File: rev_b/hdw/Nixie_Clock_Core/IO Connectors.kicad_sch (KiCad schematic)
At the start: 0 parts

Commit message: more rev b sch progress
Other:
- note added: "FIND A CONNECTOR THAT CAN HANDLE HIGH VOLTAGE AND SIGNALLING THAT ISNT AWFUL CONSIDER USING 0.1" SMT HEADERS"
- note removed: "FIND A CONNECTOR THAT CAN HANDLE HIGH VOLTAGE AND SIGNALLING THAT ISNT AWFUL"
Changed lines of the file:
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@@
     (company "Drew Maatman")
   )
-  (text "FIND A CONNECTOR THAT CAN HANDLE HIGH VOLTAGE\nAND SIGNALLING THAT ISNT AWFUL"
-    (at 59.69 43.18 0)
+  (text "FIND A CONNECTOR THAT CAN HANDLE HIGH VOLTAGE\nAND SIGNALLING THAT ISNT AWFUL\n\nCONSIDER USING 0.1\" SMT HEADERS"
+    (at 36.83 48.26 0)
     (effects (font (face "Courier New") (size 5.08 5.08) (thickness 0.254) bold (color 255 37 56 1)) (justify left bottom))
   )
+  (global_label "Colon_3_DSP" (shape output) (at 54.61 162.56 0) (fields_autoplaced)
+    (effects (font (size 1.27 1.27)) (justify left))
+    (property "Intersheetrefs" "${INTERSHEET_REFS}" (at 69.7922 162.56 0)
+      (effects (font (size 1.27 1.27)) (justify left) hide)
+    )
+  )
+  (global_label "~{Display_Detect_DSP}" (shape input) (at 54.61 134.62 0)
+    (effects (font (size 1.016 1.016)) (justify left))
+    (property "Intersheetrefs" "${INTERSHEET_REFS}" (at 54.61 134.62 0)
+      (effects (font (size 1.27 1.27)) hide)
+    )
+  )
+  (global_label "Anode_6_DSP" (shape output) (at 54.61 101.6 0) (fields_autoplaced)
+    (effects (font (size 1.27 1.27)) (justify left))
+    (property "Intersheetrefs" "${INTERSHEET_REFS}" (at 70.0342 101.6 0)
+      (effects (font (size 1.27 1.27)) (justify left) hide)
+    )
+  )
+  (global_label "Colon_0_DSP" (shape output) (at 54.61 154.94 0) (fields_autoplaced)
+    (effects (font (size 1.27 1.27)) (justify left))
+    (property "Intersheetrefs" "${INTERSHEET_REFS}" (at 69.7922 154.94 0)
+      (effects (font (size 1.27 1.27)) (justify left) hide)
+    )
+  )
+  (global_label "Anode_4_DSP" (shape output) (at 54.61 96.52 0) (fields_autoplaced)
+    (effects (font (size 1.27 1.27)) (justify left))
+    (property "Intersheetrefs" "${INTERSHEET_REFS}" (at 70.0342 96.52 0)
+      (effects (font (size 1.27 1.27)) (justify left) hide)
+    )
+  )
+  (global_label "Anode_3_DSP" (shape output) (at 54.61 93.98 0) (fields_autoplaced)
+    (effects (font (size 1.27 1.27)) (justify left))
+    (property "Intersheetrefs" "${INTERSHEET_REFS}" (at 70.0342 93.98 0)
+      (effects (font (size 1.27 1.27)) (justify left) hide)
+    )
+  )
+  (global_label "I2C_DSP_SDA" (shape output) (at 54.61 113.03 0)
+    (effects (font (size 1.27 1.27)) (justify left))
+    (property "Intersheetrefs" "${INTERSHEET_REFS}" (at 54.61 113.03 0)
+      (effects (font (size 1.27 1.27)) hide)
+    )
+  )
+  (global_label "Pushbutton_1_DSP" (shape input) (at 54.61 119.38 0) (fields_autoplaced)
+    (effects (font (size 1.27 1.27)) (justify left))
+    (property "Intersheetrefs" "${INTERSHEET_REFS}" (at 75.0535 119.38 0)
+      (effects (font (size 1.27 1.27)) (justify left) hide)
+    )
+  )
+  (global_label "Pushbutton_4_DSP" (shape input) (at 54.61 127 0) (fields_autoplaced)
+    (effects (font (size 1.27 1.27)) (justify left))
+    (property "Intersheetrefs" "${INTERSHEET_REFS}" (at 75.0535 127 0)
+      (effects (font (size 1.27 1.27)) (justify left) hide)
+    )
+  )
+  (global_label "Pushbutton_5_DSP" (shape input) (at 54.61 129.54 0) (fields_autoplaced)
+    (effects (font (size 1.27 1.27)) (justify left))
+    (property "Intersheetrefs" "${INTERSHEET_REFS}" (at 75.0535 129.54 0)
+      (effects (font (size 1.27 1.27)) (justify left) hide)
+    )
+  )
+  (global_label "Anode_9_DSP" (shape output) (at 54.61 149.86 0) (fields_autoplaced)
+    (effects (font (size 1.27 1.27)) (justify left))
+    (property "Intersheetrefs" "${INTERSHEET_REFS}" (at 70.0342 149.86 0)
+      (effects (font (size 1.27 1.27)) (justify left) hide)
+    )
+  )
+  (global_label "Anode_2_DSP" (shape output) (at 54.61 91.44 0) (fields_autoplaced)
+    (effects (font (size 1.27 1.27)) (justify left))
+    (property "Intersheetrefs" "${INTERSHEET_REFS}" (at 70.0342 91.44 0)
+      (effects (font (size 1.27 1.27)) (justify left) hide)
+    )
+  )
+  (global_label "Pushbutton_0_DSP" (shape input) (at 54.61 116.84 0) (fields_autoplaced)
+    (effects (font (size 1.27 1.27)) (justify left))
+    (property "Intersheetrefs" "${INTERSHEET_REFS}" (at 75.0535 116.84 0)
+      (effects (font (size 1.27 1.27)) (justify left) hide)
+    )
+  )
+  (global_label "Anode_8_DSP" (shape output) (at 54.61 147.32 0) (fields_autoplaced)
+    (effects (font (size 1.27 1.27)) (justify left))
+    (property "Intersheetrefs" "${INTERSHEET_REFS}" (at 70.0342 147.32 0)
+      (effects (font (size 1.27 1.27)) (justify left) hide)
+    )
+  )
+  (global_label "Anode_5_DSP" (shape output) (at 54.61 99.06 0) (fields_autoplaced)
+    (effects (font (size 1.27 1.27)) (justify left))
+    (property "Intersheetrefs" "${INTERSHEET_REFS}" (at 70.0342 99.06 0)
+      (effects (font (size 1.27 1.27)) (justify left) hide)
+    )
+  )
+  (global_label "Anode_7_DSP" (shape output) (at 54.61 104.14 0) (fields_autoplaced)
+    (effects (font (size 1.27 1.27)) (justify left))
+    (property "Intersheetrefs" "${INTERSHEET_REFS}" (at 70.0342 104.14 0)
+      (effects (font (size 1.27 1.27)) (justify left) hide)
+    )
+  )
+  (global_label "Pushbutton_6_DSP" (shape input) (at 54.61 132.08 0) (fields_autoplaced)
+    (effects (font (size 1.27 1.27)) (justify left))
+    (property "Intersheetrefs" "${INTERSHEET_REFS}" (at 75.0535 132.08 0)
+      (effects (font (size 1.27 1.27)) (justify left) hide)
+    )
+  )
+  (global_label "Pushbutton_2_DSP" (shape input) (at 54.61 121.92 0) (fields_autoplaced)
+    (effects (font (size 1.27 1.27)) (justify left))
+    (property "Intersheetrefs" "${INTERSHEET_REFS}" (at 75.0535 121.92 0)
+      (effects (font (size 1.27 1.27)) (justify left) hide)
+    )
+  )
+  (global_label "Colon_1_DSP" (shape output) (at 54.61 157.48 0) (fields_autoplaced)
+    (effects (font (size 1.27 1.27)) (justify left))
+    (property "Intersheetrefs" "${INTERSHEET_REFS}" (at 69.7922 157.48 0)
+      (effects (font (size 1.27 1.27)) (justify left) hide)
+    )
+  )
+  (global_label "I2C_DSP_SCL" (shape output) (at 54.61 110.49 0)
+    (effects (font (size 1.27 1.27)) (justify left))
+    (property "Intersheetrefs" "${INTERSHEET_REFS}" (at 54.61 110.49 0)
+      (effects (font (size 1.27 1.27)) hide)
+    )
+  )
+  (global_label "Colon_2_DSP" (shape output) (at 54.61 160.02 0) (fields_autoplaced)
+    (effects (font (size 1.27 1.27)) (justify left))
+    (property "Intersheetrefs" "${INTERSHEET_REFS}" (at 69.7922 160.02 0)
+      (effects (font (size 1.27 1.27)) (justify left) hide)
+    )
+  )
+  (global_label "Anode_1_DSP" (shape output) (at 54.61 88.9 0) (fields_autoplaced)
+    (effects (font (size 1.27 1.27)) (justify left))
+    (property "Intersheetrefs" "${INTERSHEET_REFS}" (at 70.0342 88.9 0)
+      (effects (font (size 1.27 1.27)) (justify left) hide)
+    )
+  )
+  (global_label "Anode_DP_DSP" (shape output) (at 54.61 152.4 0) (fields_autoplaced)
+    (effects (font (size 1.27 1.27)) (justify left))
+    (property "Intersheetrefs" "${INTERSHEET_REFS}" (at 71.3647 152.4 0)
+      (effects (font (size 1.27 1.27)) (justify left) hide)
+    )
+  )
+  (global_label "Anode_0_DSP" (shape output) (at 54.61 86.36 0) (fields_autoplaced)
+    (effects (font (size 1.27 1.27)) (justify left))
+    (property "Intersheetrefs" "${INTERSHEET_REFS}" (at 70.0342 86.36 0)
+      (effects (font (size 1.27 1.27)) (justify left) hide)
+    )
+  )
+  (global_label "Pushbutton_3_DSP" (shape input) (at 54.61 124.46 0) (fields_autoplaced)
+    (effects (font (size 1.27 1.27)) (justify left))
+    (property "Intersheetrefs" "${INTERSHEET_REFS}" (at 75.0535 124.46 0)
+      (effects (font (size 1.27 1.27)) (justify left) hide)
+    )
+  )
+  (symbol (lib_id "Custom Library:+90V") (at 125.73 104.14 0) (unit 1)
+    (in_bom yes) (on_board yes) (dnp no) (fields_autoplaced)
+    (property "Reference" "#PWR?" (at 125.73 107.95 0)
+      (effects (font (size 1.27 1.27)) hide)
+    )
+    (property "Value" "+90V" (at 125.73 100.33 0)
+      (effects (font (size 1.27 1.27)))
+    )
+    (property "Footprint" "" (at 125.73 104.14 0)
+      (effects (font (size 1.524 1.524)))
+    )
+    (property "Datasheet" "" (at 125.73 104.14 0)
+      (effects (font (size 1.524 1.524)))
+    )
+    (pin "1")
+    (instances
+      (project "Nixie_Clock_Core"
+        (path "/16fdce21-b570-4d81-a458-e8839d611806/0b6dccc1-0a92-424d-9916-2441ea7dc052"
+          (reference "#PWR?") (unit 1)
+        )
+        (path "/16fdce21-b570-4d81-a458-e8839d611806/2e22fd27-425d-47fb-8810-3fe495af3afd"
+          (reference "#PWR01901") (unit 1)
+        )
+      )
+    )
+  )
+  (symbol (lib_id "Custom Library:+180") (at 134.62 104.14 0) (unit 1)
+    (in_bom yes) (on_board yes) (dnp no) (fields_autoplaced)
+    (property "Reference" "#PWR?" (at 134.62 107.95 0)
+      (effects (font (size 1.27 1.27)) hide)
+    )
+    (property "Value" "+180V" (at 134.62 100.33 0)
+      (effects (font (size 1.27 1.27)))
+    )
+    (property "Footprint" "" (at 134.62 104.14 0)
+      (effects (font (size 1.524 1.524)))
+    )
+    (property "Datasheet" "" (at 134.62 104.14 0)
+      (effects (font (size 1.524 1.524)))
+    )
+    (pin "1")
+    (instances
+      (project "Nixie_Clock_Core"
+        (path "/16fdce21-b570-4d81-a458-e8839d611806/0b6dccc1-0a92-424d-9916-2441ea7dc052"
+          (reference "#PWR?") (unit 1)
+        )
+        (path "/16fdce21-b570-4d81-a458-e8839d611806/2e22fd27-425d-47fb-8810-3fe495af3afd"
+          (reference "#PWR01902") (unit 1)
+        )
+      )
+    )
+  )
 )

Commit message: more carrier board progress
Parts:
- added J?: Conn_02x30_Odd_Even, symbol Connector_Generic:Conn_02x30_Odd_Even
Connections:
- net +180V: now also J?.1 (Pin_1), J?.3 (Pin_3), J?.7 (Pin_7), J?.9 (Pin_9)
- net Anode_0_DSP: now also J?.13 (Pin_13)
- net Anode_1_DSP: now also J?.14 (Pin_14)
- net Anode_2_DSP: now also J?.15 (Pin_15)
- net Anode_3_DSP: now also J?.16 (Pin_16)
- net Anode_4_DSP: now also J?.17 (Pin_17)
- net Anode_5_DSP: now also J?.18 (Pin_18)
- net Colon_0_DSP: now also J?.35 (Pin_35)
- net Colon_1_DSP: now also J?.36 (Pin_36)
- net Colon_2_DSP: now also J?.37 (Pin_37)
- net Colon_3_DSP: now also J?.38 (Pin_38)
- net I2C_DSP_SCL: now also J?.51 (Pin_51)
- net I2C_DSP_SDA: now also J?.52 (Pin_52)
- net Pushbutton_0_DSP: now also J?.41 (Pin_41)
- net Pushbutton_1_DSP: now also J?.42 (Pin_42)
- net Pushbutton_2_DSP: now also J?.43 (Pin_43)
- net Pushbutton_3_DSP: now also J?.44 (Pin_44)
- net Pushbutton_4_DSP: now also J?.45 (Pin_45)
- net Pushbutton_5_DSP: now also J?.46 (Pin_46)
- net Pushbutton_6_DSP: now also J?.47 (Pin_47)
- net ~{Display_Detect_DSP}: now also J?.49 (Pin_49)
- new net +3.3V: J?.53 (Pin_53), J?.55 (Pin_55), J?.57 (Pin_57), J?.59 (Pin_59)
- new net Cathode_0_DSP: J?.21 (Pin_21)
- new net Cathode_1_DSP: J?.22 (Pin_22)
- new net Cathode_2_DSP: J?.23 (Pin_23)
- new net Cathode_3_DSP: J?.24 (Pin_24)
- new net Cathode_4_DSP: J?.25 (Pin_25)
- new net Cathode_5_DSP: J?.26 (Pin_26)
- new net Cathode_6_DSP: J?.27 (Pin_27)
- new net Cathode_7_DSP: J?.28 (Pin_28)
- new net Cathode_8_DSP: J?.29 (Pin_29)
- new net Cathode_9_DSP: J?.30 (Pin_30)
- new net Cathode_DP_DSP: J?.31 (Pin_31)
- new net GND: J?.10 (Pin_10), J?.11 (Pin_11), J?.12 (Pin_12), J?.19 (Pin_19), J?.2 (Pin_2), J?.20 (Pin_20), J?.32 (Pin_32), J?.33 (Pin_33), J?.34 (Pin_34), J?.39 (Pin_39), J?.4 (Pin_4), J?.40 (Pin_40), J?.48 (Pin_48), J?.50 (Pin_50), J?.54 (Pin_54), J?.56 (Pin_56), J?.58 (Pin_58), J?.6 (Pin_6), J?.60 (Pin_60), J?.8 (Pin_8)
- no-connect marks 0 -> 1
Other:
- note added: "ADD BYPASS"

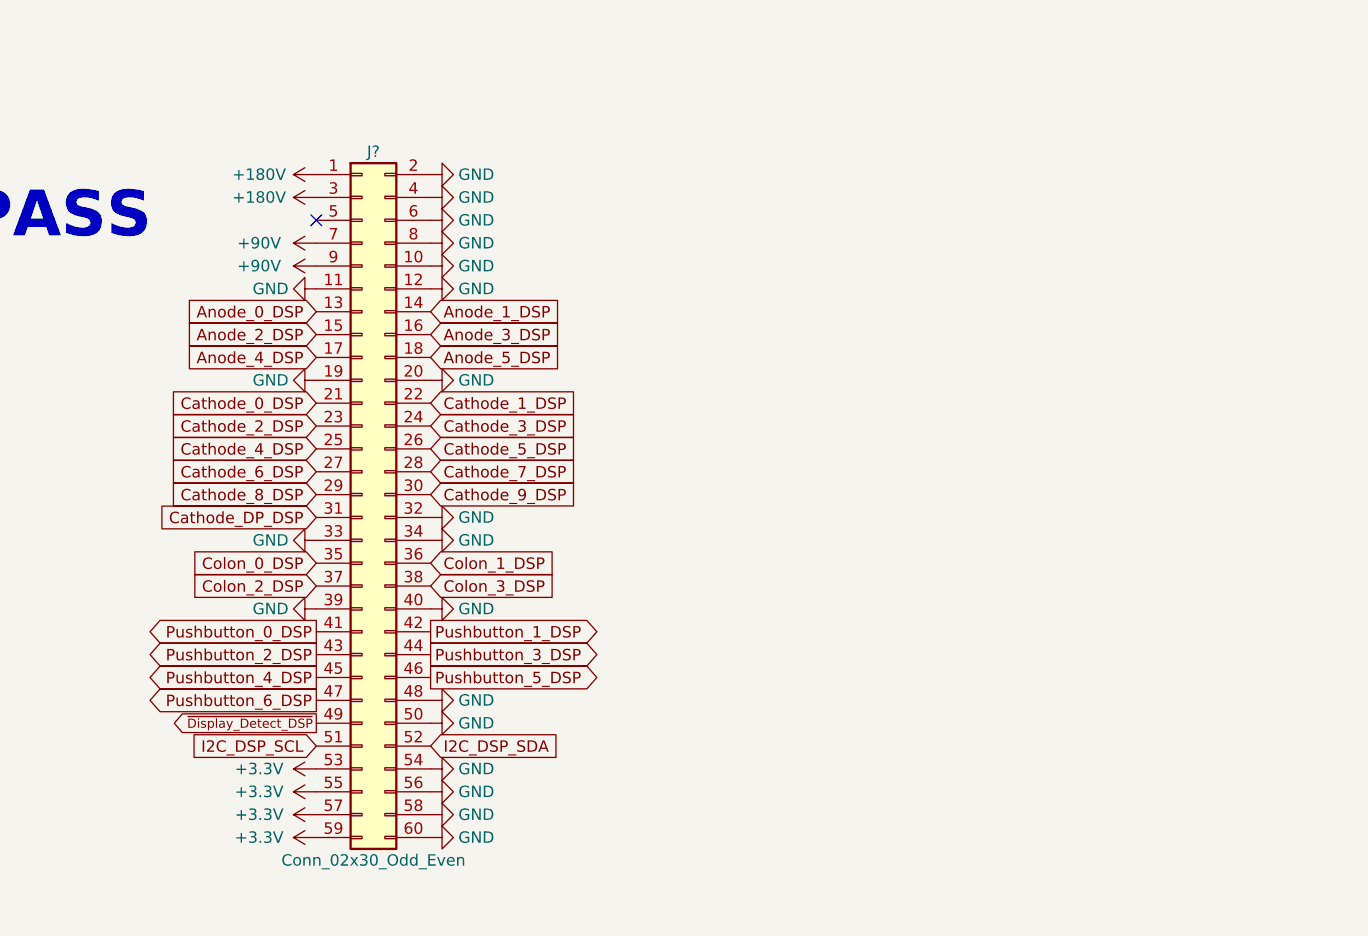
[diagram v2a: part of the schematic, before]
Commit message: more schematic progress, assigning signals to MCU"
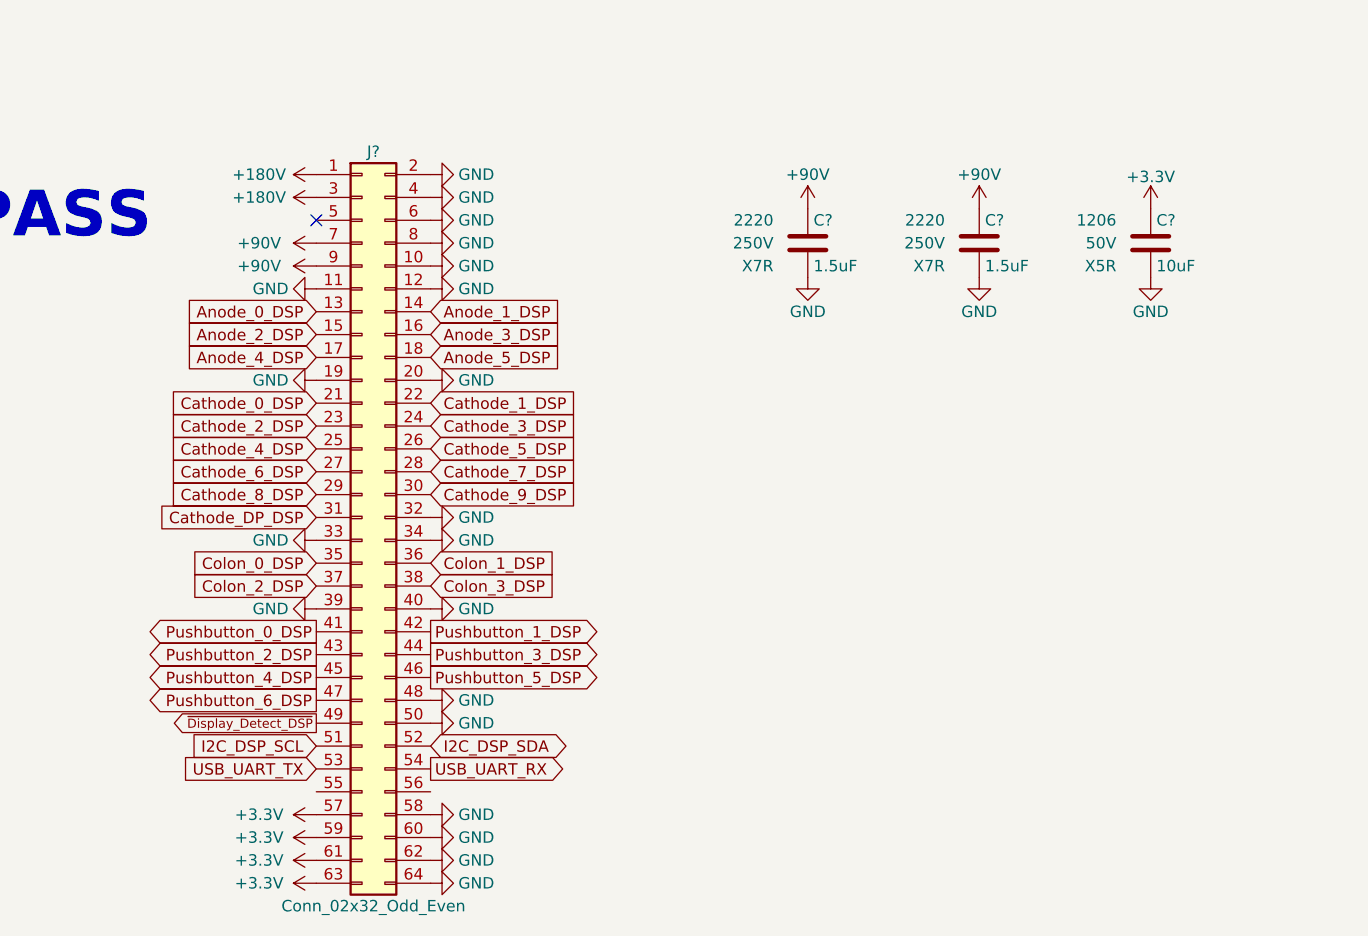
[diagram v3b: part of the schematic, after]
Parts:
- removed J?: Conn_02x30_Odd_Even, symbol Connector_Generic:Conn_02x30_Odd_Even
- added C? (x2): 1.5uF, symbol Custom Library:C_Custom
- added C?: 10uF, symbol Custom Library:C_Custom
- added J?: Conn_02x32_Odd_Even, symbol Connector_Generic:Conn_02x32_Odd_Even
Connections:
- net +180V: now also J?.1 (Pin_1), J?.3 (Pin_3), J?.7 (Pin_7), J?.9 (Pin_9)
- net +3.3V: now also C?.1, J?.57 (Pin_57), J?.59 (Pin_59), J?.61 (Pin_61), J?.63 (Pin_63)
- net Anode_0_DSP: now also J?.13 (Pin_13)
- net Anode_1_DSP: now also J?.14 (Pin_14)
- net Anode_2_DSP: now also J?.15 (Pin_15)
- net Anode_3_DSP: now also J?.16 (Pin_16)
- net Anode_4_DSP: now also J?.17 (Pin_17)
- net Anode_5_DSP: now also J?.18 (Pin_18)
- net Cathode_0_DSP: now also J?.21 (Pin_21)
- net Cathode_1_DSP: now also J?.22 (Pin_22)
- net Cathode_2_DSP: now also J?.23 (Pin_23)
- net Cathode_3_DSP: now also J?.24 (Pin_24)
- net Cathode_4_DSP: now also J?.25 (Pin_25)
- net Cathode_5_DSP: now also J?.26 (Pin_26)
- net Cathode_6_DSP: now also J?.27 (Pin_27)
- net Cathode_7_DSP: now also J?.28 (Pin_28)
- net Cathode_8_DSP: now also J?.29 (Pin_29)
- net Cathode_9_DSP: now also J?.30 (Pin_30)
- net Cathode_DP_DSP: now also J?.31 (Pin_31)
- net Colon_0_DSP: now also J?.35 (Pin_35)
- net Colon_1_DSP: now also J?.36 (Pin_36)
- net Colon_2_DSP: now also J?.37 (Pin_37)
- net Colon_3_DSP: now also J?.38 (Pin_38)
- net GND: now also C?.2, C?.2, C?.2, J?.10 (Pin_10), J?.11 (Pin_11), J?.12 (Pin_12), J?.19 (Pin_19), J?.2 (Pin_2), J?.20 (Pin_20), J?.32 (Pin_32), J?.33 (Pin_33), J?.34 (Pin_34), J?.39 (Pin_39), J?.4 (Pin_4), J?.40 (Pin_40), J?.48 (Pin_48), J?.50 (Pin_50), J?.58 (Pin_58), J?.6 (Pin_6), J?.60 (Pin_60), J?.62 (Pin_62), J?.64 (Pin_64), J?.8 (Pin_8)
- net I2C_DSP_SCL: now also J?.51 (Pin_51)
- net I2C_DSP_SDA: now also J?.52 (Pin_52)
- net Pushbutton_0_DSP: now also J?.41 (Pin_41)
- net Pushbutton_1_DSP: now also J?.42 (Pin_42)
- net Pushbutton_2_DSP: now also J?.43 (Pin_43)
- net Pushbutton_3_DSP: now also J?.44 (Pin_44)
- net Pushbutton_4_DSP: now also J?.45 (Pin_45)
- net Pushbutton_5_DSP: now also J?.46 (Pin_46)
- net Pushbutton_6_DSP: now also J?.47 (Pin_47)
- net ~{Display_Detect_DSP}: now also J?.49 (Pin_49)
- new net +90V: C?.1, C?.1
- new net USB_UART_RX: J?.54 (Pin_54)
- new net USB_UART_TX: J?.53 (Pin_53)
